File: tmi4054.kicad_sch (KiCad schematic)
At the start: 16 parts, among them J1 USB_C_Receptacle_USB2.0, J2 Conn_01x02_Male, J3 Conn_01x02_Male, Q1 AO3401, SW1 SW_SPDT, U1 LTC4054ES5-4.2

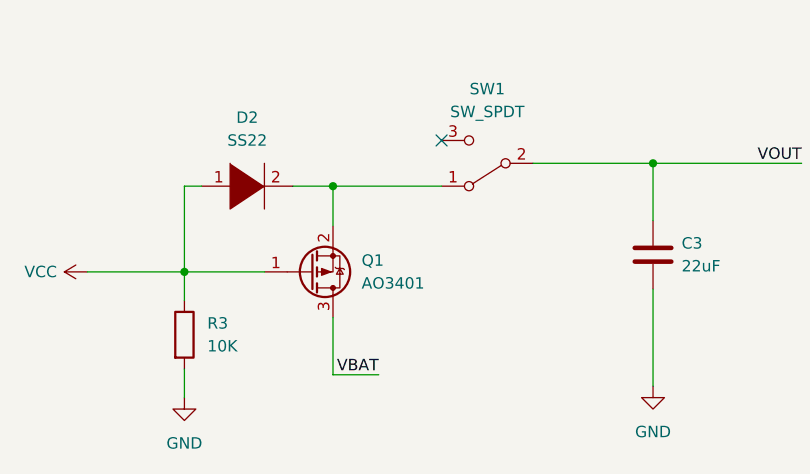
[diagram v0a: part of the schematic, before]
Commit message: adjust pmos model to AO3401A
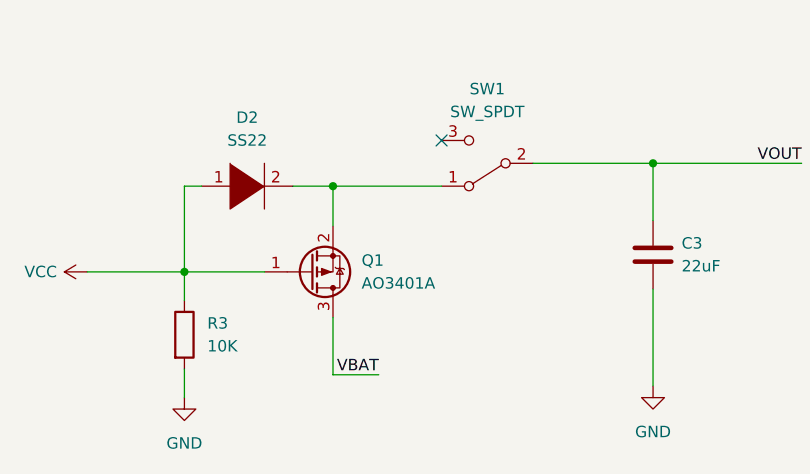
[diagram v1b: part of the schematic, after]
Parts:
- removed Q1: AO3401, Package_TO_SOT_SMD:SOT-23, symbol Device:Q_PMOS_GSD
- added Q1: AO3401A, Package_TO_SOT_SMD:SOT-23, symbol Transistor_FET:AO3401A
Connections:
- net VBAT: now also Q1.3 (D)
- net VCC: now also Q1.1 (G)
- net at D2.2 (A), SW1.1 (A): now also Q1.2 (S)
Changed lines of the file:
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@@
     (pin "1")
+  )
+  (symbol (lib_id "Transistor_FET:AO3401A") (at 222.25 161.925 0) (mirror x) (unit 1)
+    (in_bom yes) (on_board yes) (fields_autoplaced)
+    (property "Reference" "Q1" (id 0) (at 227.965 160.6549 0)
+      (effects (font (size 1.27 1.27)) (justify left))
+    )
+    (property "Value" "AO3401A" (id 1) (at 227.965 163.1949 0)
+      (effects (font (size 1.27 1.27)) (justify left))
+    )
+    (property "Footprint" "Package_TO_SOT_SMD:SOT-23" (id 2) (at 227.33 160.02 0)
+      (effects (font (size 1.27 1.27) italic) (justify left) hide)
+    )
+    (property "Datasheet" "http://www.aosmd.com/pdfs/datasheet/AO3401A.pdf" (id 3) (at 222.25 161.925 0)
+      (effects (font (size 1.27 1.27)) (justify left) hide)
+    )
+    (pin "1")
+    (pin "2")
+    (pin "3")
   )
   (symbol (lib_id "power:VCC") (at 203.2 105.41 90) (unit 1)
@@
     (pin "1")
   )
-  (symbol (lib_id "Device:Q_PMOS_GSD") (at 222.25 161.925 0) (mirror x) (unit 1)
-    (in_bom yes) (on_board yes) (fields_autoplaced)
-    (property "Reference" "Q1" (id 0) (at 227.965 160.6549 0)
-      (effects (font (size 1.27 1.27)) (justify left))
-    )
-    (property "Value" "AO3401" (id 1) (at 227.965 163.1949 0)
-      (effects (font (size 1.27 1.27)) (justify left))
-    )
-    (property "Footprint" "Package_TO_SOT_SMD:SOT-23" (id 2) (at 227.33 164.465 0)
-      (effects (font (size 1.27 1.27)) hide)
-    )
-    (property "Datasheet" "~" (id 3) (at 222.25 161.925 0)
-      (effects (font (size 1.27 1.27)) hide)
-    )
-    (pin "1")
-    (pin "2")
-    (pin "3")
-  )
   (symbol (lib_id "pspice:DIODE") (at 215.265 152.4 0) (unit 1)
     (in_bom yes) (on_board yes) (fields_autoplaced)
@@
       (reference "J3") (unit 1) (value "Conn_01x02_Male") (footprint "Connector_PinHeader_2.54mm:PinHeader_1x02_P2.54mm_Vertical")
     )
-    (path "/6eea67fa-7dab-4df3-b34d-bf4d7e455930"
-      (reference "Q1") (unit 1) (value "AO3401") (footprint "Package_TO_SOT_SMD:SOT-23")
+    (path "/36099039-1e5f-4dd4-b4a3-0f472df3d86e"
+      (reference "Q1") (unit 1) (value "AO3401A") (footprint "Package_TO_SOT_SMD:SOT-23")
     )
     (path "/521e0795-0a91-4e1b-bf38-ca065cd6aa43"
